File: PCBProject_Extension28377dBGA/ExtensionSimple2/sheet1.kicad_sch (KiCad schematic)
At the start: 109 parts, among them J1 Conn_02x05_Odd_Even, J1 Conn_02x08_Top_Bottom, J2 Conn_01x02_Pin, J5 RS485_1_CONNECT, J7 RS485_2_CONNECT, Q1 FMMT618TA, U1 SN74ABT541, U2 SN74ABT541, U3 SN65HVD75D

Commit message: 解决电流传感器中的错误：电线与边缘太近了！
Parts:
- added C15: 104, Capacitor_SMD:C_0805_2012Metric, symbol sheet1-altium-import:root_1_Cap
- added R48: 4.7k, Resistor_SMD:R_0805_2012Metric, symbol sheet1-altium-import:root_1_Res2
- added U4: SN65HVD230, Package_SO:SOIC-8_3.9x4.9mm_P1.27mm, symbol Interface_CAN_LIN:SN65HVD230
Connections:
- net AGND: now also C15.2, R48.2, U4.2 (GND); no longer C1.1
- net DSP_A_CAN_RX: now also U4.4 (R)
- net DSP_A_CAN_TX: now also U4.1 (D)
- net DSP_PWM1~{_ENABL}E: no longer C1.2
- net VDD: now also C15.1, U4.3 (VCC)
- new net: R48.1, U4.8 (Rs)
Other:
- moved on the sheet: C1

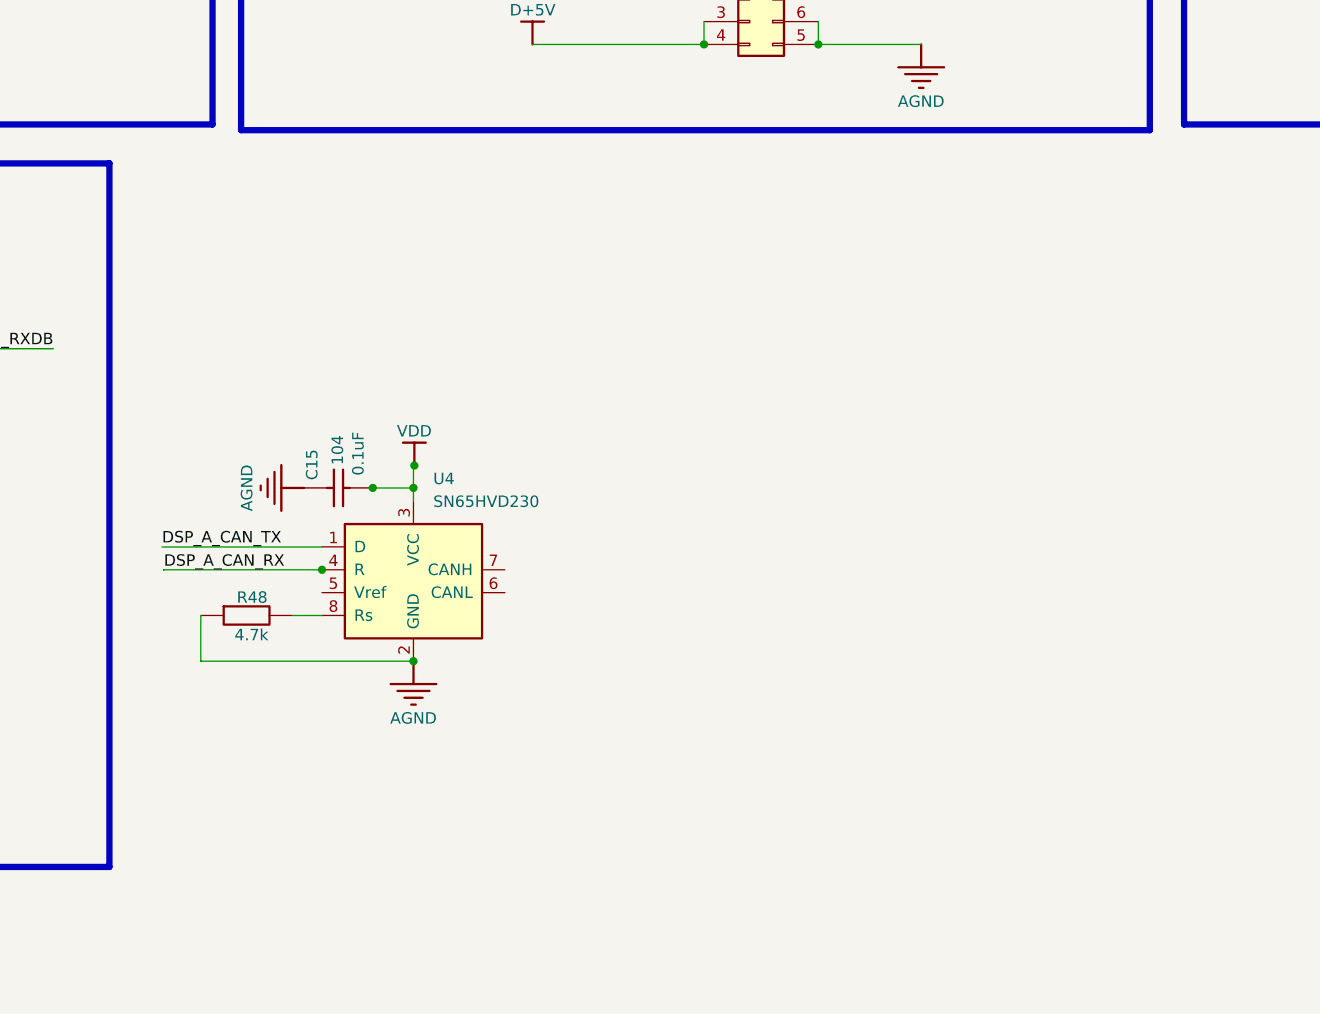
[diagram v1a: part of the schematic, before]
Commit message: 底板中增加了CAN转TTL模块，并初步修改了底板的尺寸
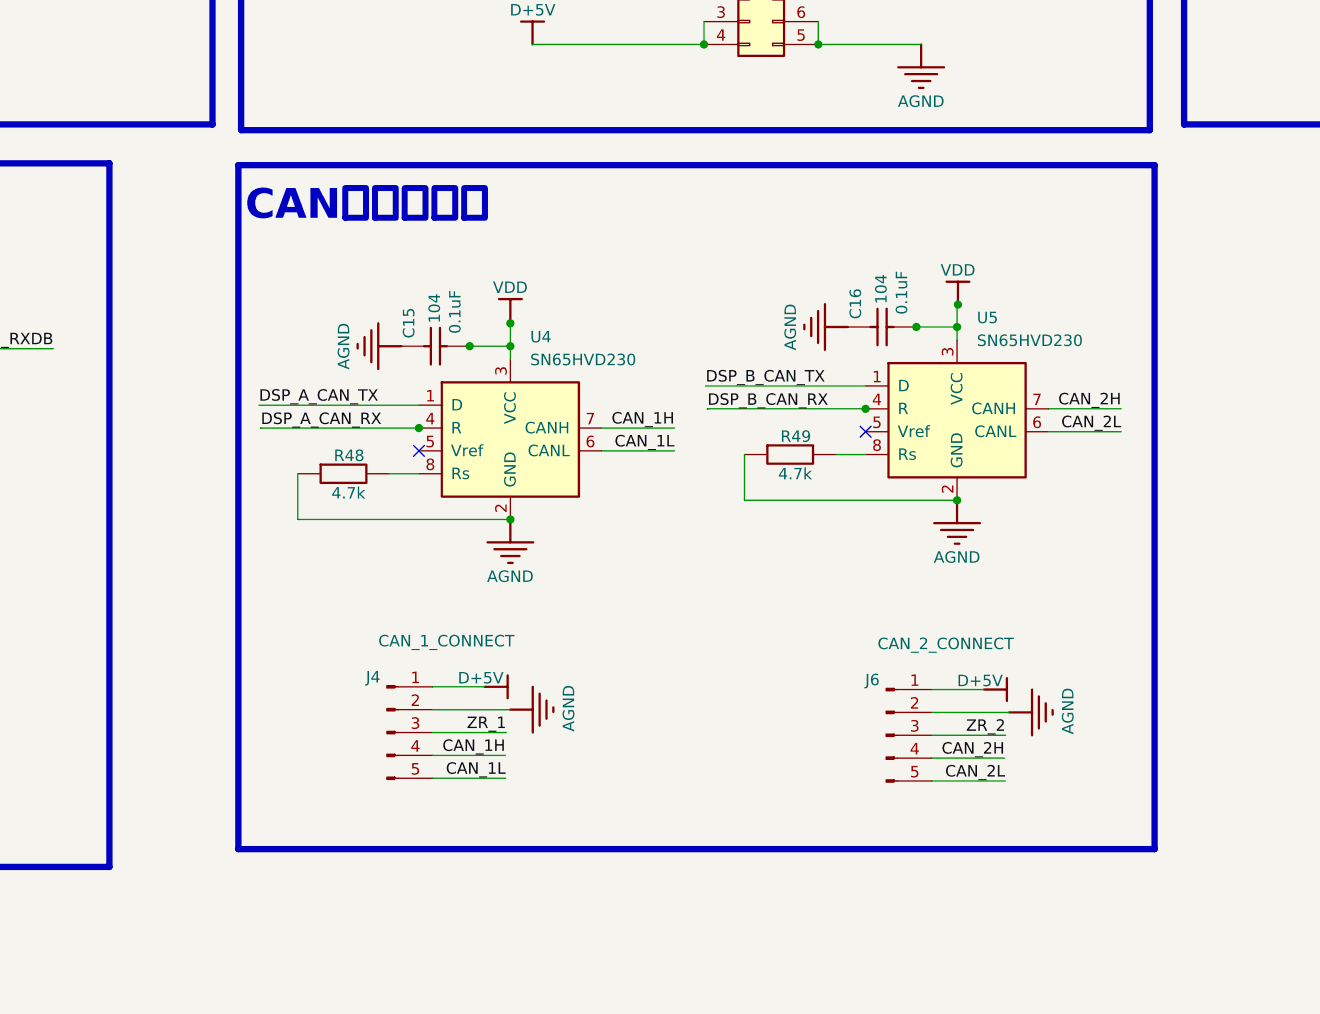
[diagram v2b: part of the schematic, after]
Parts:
- added C16: 104, Capacitor_SMD:C_0805_2012Metric, symbol sheet1-altium-import:root_1_Cap
- added J4: CAN_1_CONNECT, Connector_PinSocket_2.54mm:PinSocket_1x05_P2.54mm_Vertical, symbol Connector:Conn_01x05_Pin
- added J6: CAN_2_CONNECT, Connector_PinSocket_2.54mm:PinSocket_1x05_P2.54mm_Vertical, symbol Connector:Conn_01x05_Pin
- added R49: 4.7k, Resistor_SMD:R_0805_2012Metric, symbol sheet1-altium-import:root_1_Res2
- added U5: SN65HVD230, Package_SO:SOIC-8_3.9x4.9mm_P1.27mm, symbol Interface_CAN_LIN:SN65HVD230
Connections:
- net AGND: now also C16.2, J4.2 (Pin_2), J6.2 (Pin_2), R49.2, U5.2 (GND)
- net D+5V: now also J4.1 (Pin_1), J6.1 (Pin_1)
- net DSP_B_CAN_RX: now also U5.4 (R)
- net DSP_B_CAN_TX: now also U5.1 (D)
- net VDD: now also C16.1, U5.3 (VCC)
- net CAN_1L: now reaches U4.6 (CANL)
- net CAN_1L: now also J4.5 (Pin_5)
- net CAN_1H: now reaches U4.7 (CANH)
- net CAN_1H: now also J4.4 (Pin_4)
- new net: R49.1, U5.8 (Rs)
- new net CAN_2H: J6.4 (Pin_4), U5.7 (CANH)
- new net CAN_2L: J6.5 (Pin_5), U5.6 (CANL)
- new net ZR_1: J4.3 (Pin_3)
- new net ZR_2: J6.3 (Pin_3)
- no-connect marks 84 -> 86
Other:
- note added: "CAN编码器通讯"
- moved on the sheet: C15, R48, U4

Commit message: 确定底板尺寸，目前只差布线
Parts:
- DSP1: footprint Oshinoko:DSP_240_0p6mm -> 1mmlab_pcb_lib:DSP_240_SMD
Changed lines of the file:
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@@
       (effects (font (size 1.27 1.27)))
     )
-    (property "Footprint" "Oshinoko:DSP_240_0p6mm" (at 711.2 421.64 0)
+    (property "Footprint" "1mmlab_pcb_lib:DSP_240_SMD" (at 711.2 421.64 0)
       (effects (font (size 1.27 1.27)) hide)
     )

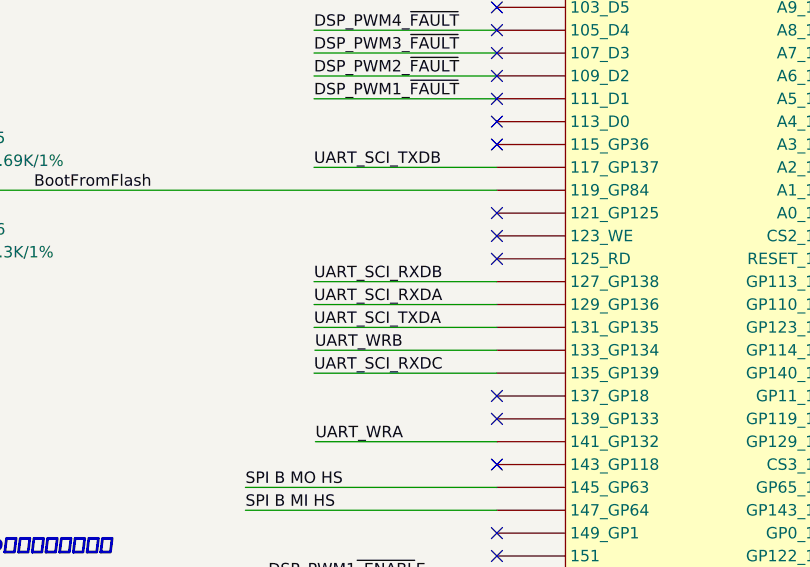
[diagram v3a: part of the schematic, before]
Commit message: 底板布线基本完毕，但是还有些地方出现了混乱，仍需改进
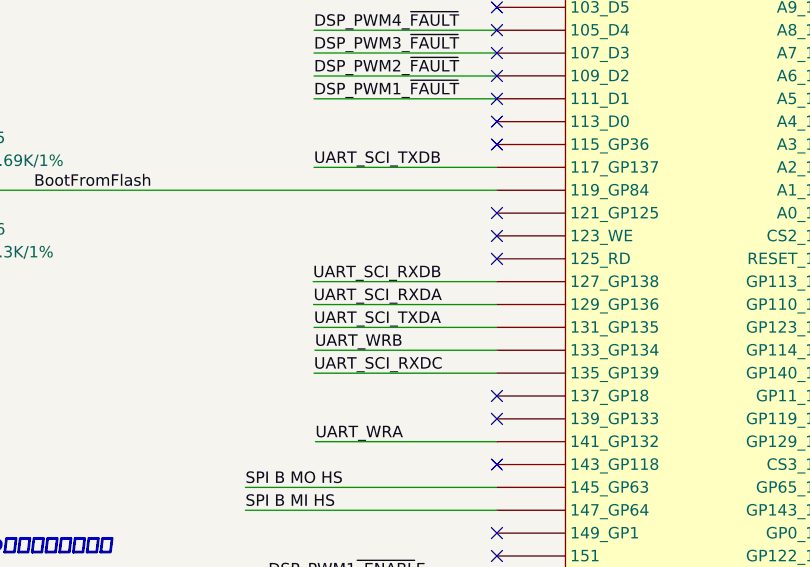
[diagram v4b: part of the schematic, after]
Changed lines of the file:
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@@
+    (stroke (width 0) (type default))
+  )
+  (wire (pts (xy 690.7784 591.82) (xy 711.2 591.82))
     (stroke (width 0) (type default))
   )
@@
     (stroke (width 0.254) (type default))
   )
-  (wire (pts (xy 711.2 594.36) (xy 690.88 594.36))
-    (stroke (width 0.254) (type default))
-  )
   (wire (pts (xy 374.65 70.485) (xy 384.81 70.485))
     (stroke (width 0.254) (type default))
@@
     (stroke (width 0.254) (type default))
   )
+  (wire (pts (xy 690.8292 594.36) (xy 711.2 594.36))
+    (stroke (width 0) (type default))
+  )
   (wire (pts (xy 579.12 268.605) (xy 589.28 268.605))
     (stroke (width 0.254) (type default))
@@
   (wire (pts (xy 346.71 360.045) (xy 346.71 362.585))
     (stroke (width 0) (type default))
-  )
-  (wire (pts (xy 711.2 591.82) (xy 690.88 591.82))
-    (stroke (width 0.254) (type default))
   )
   (wire (pts (xy 756.92 675.64) (xy 770.255 675.64))
@@
     (effects (font (size 1.27 1.27)) (justify left bottom))
   )
+  (label "UART_SCI_RXDA" (at 690.8292 594.36 0) (fields_autoplaced)
+    (effects (font (size 1.27 1.27)) (justify left bottom))
+  )
   (label "RS485_2_B" (at 588.3148 378.6886 180) (fields_autoplaced)
     (effects (font (size 1.27 1.27)) (justify right bottom))
@@
     (effects (font (size 1.27 1.27)) (justify right bottom))
   )
-  (label "UART_SCI_RXDA" (at 690.88 594.36 180) (fields_autoplaced)
-    (effects (font (size 1.27 1.27)) (justify left bottom))
-  )
-  (label "UART_SCI_RXDB" (at 690.88 591.82 180) (fields_autoplaced)
-    (effects (font (size 1.27 1.27)) (justify left bottom))
-  )
   (label "IPM_VDC_BUS1" (at 448.31 67.945 180) (fields_autoplaced)
     (effects (font (size 1.27 1.27)) (justify left bottom))
@@
     (effects (font (size 1.27 1.27)) (justify right bottom))
   )
+  (label "UART_SCI_RXDB" (at 690.7784 591.82 0) (fields_autoplaced)
+    (effects (font (size 1.27 1.27)) (justify left bottom))
+  )
   (label "DSP_B_CAN_TX" (at 693.42 462.28 180) (fields_autoplaced)

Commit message: 底板布线完毕！
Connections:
- net AGND: now also C1.1
- net DSP_PWM1~{_ENABL}E: now also C1.2
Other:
- moved on the sheet: C1
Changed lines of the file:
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@@
   (junction (at 520.7 129.54) (diameter 0) (color 0 0 0 0)
   )
+  (junction (at 106.4006 61.468) (diameter 0) (color 0 0 0 0)
+  )
   (junction (at 520.7 132.08) (diameter 0) (color 0 0 0 0)
   )
@@
     (stroke (width 0) (type default))
   )
+  (wire (pts (xy 115.1382 62.7126) (xy 114.0206 62.7126))
+    (stroke (width 0) (type default))
+  )
   (wire (pts (xy 556.9966 360.7054) (xy 556.9966 360.7562))
     (stroke (width 0) (type default))
   )
+  (wire (pts (xy 81.026 61.468) (xy 106.4006 61.468))
+    (stroke (width 0) (type default))
+  )
   (wire (pts (xy 756.92 629.92) (xy 756.92 632.46))
     (stroke (width 0.254) (type default))
@@
     (stroke (width 0.254) (type default))
   )
+  (wire (pts (xy 114.0206 62.7126) (xy 114.0206 61.468))
+    (stroke (width 0) (type default))
+  )
   (wire (pts (xy 665.48 264.16) (xy 683.26 264.16))
     (stroke (width 0.254) (type default))
@@
     (stroke (width 0) (type default))
   )
+  (wire (pts (xy 106.4006 61.468) (xy 106.426 61.468))
+    (stroke (width 0) (type default))
+  )
   (wire (pts (xy 158.75 140.335) (xy 106.68 140.335))
     (stroke (width 0.254) (type default))
@@
     (effects (font (size 1.27 1.27)) (justify right bottom))
   )
+  (label "DSP_PWM1~{_ENABL}E" (at 81.026 61.468 180) (fields_autoplaced)
+    (effects (font (size 1.27 1.27)) (justify left bottom))
+  )
   (label "DSP-PWM6B" (at 146.05 161.925 180) (fields_autoplaced)
     (effects (font (size 1.27 1.27)) (justify left bottom))
@@
     )
   )
-  (symbol (lib_id "sheet1-altium-import:root_1_Cap") (at 104.14 64.135 90) (unit 1)
+  (symbol (lib_id "sheet1-altium-import:root_1_Cap") (at 111.4806 64.008 90) (unit 1)
     (in_bom yes) (on_board yes) (dnp no)
-    (property "Reference" "C1" (at 103.886 59.309 0)
+    (property "Reference" "C1" (at 109.5502 59.8932 90)
       (effects (font (size 1.27 1.27)) (justify left bottom))
     )
-    (property "Value" "104" (at 106.426 59.309 0)
+    (property "Value" "104" (at 112.4966 66.6242 90)
       (effects (font (size 1.27 1.27)) (justify left bottom))
     )
-    (property "Footprint" "Capacitor_SMD:C_0805_2012Metric" (at 104.14 64.135 0)
+    (property "Footprint" "Capacitor_SMD:C_0805_2012Metric" (at 111.4806 64.008 0)
       (effects (font (size 1.27 1.27)) hide)
     )
-    (property "Datasheet" "" (at 104.14 64.135 0)
+    (property "Datasheet" "" (at 111.4806 64.008 0)
       (effects (font (size 1.27 1.27)) hide)
     )
-    (property "PUBLISHED" "8-Jun-2000" (at 98.552 63.881 0)
+    (property "PUBLISHED" "8-Jun-2000" (at 105.8926 63.754 0)
       (effects (font (size 1.27 1.27)) (justify left bottom) hide)
     )
-    (property "LATESTREVISIONDATE" "17-Jul-2002" (at 98.552 63.881 0)
+    (property "LATESTREVISIONDATE" "17-Jul-2002" (at 105.8926 63.754 0)
       (effects (font (size 1.27 1.27)) (justify left bottom) hide)
     )
-    (property "LATESTREVISIONNOTE" "Re-released for DXP Platform." (at 98.552 63.881 0)
+    (property "LATESTREVISIONNOTE" "Re-released for DXP Platform." (at 105.8926 63.754 0)
       (effects (font (size 1.27 1.27)) (justify left bottom) hide)
     )
-    (property "PACKAGEREFERENCE" "RAD-0.3" (at 98.552 63.881 0)
+    (property "PACKAGEREFERENCE" "RAD-0.3" (at 105.8926 63.754 0)
       (effects (font (size 1.27 1.27)) (justify left bottom) hide)
     )
-    (property "PUBLISHER" "Altium Limited" (at 98.552 63.881 0)
+    (property "PUBLISHER" "Altium Limited" (at 105.8926 63.754 0)
       (effects (font (size 1.27 1.27)) (justify left bottom) hide)
     )
-    (property "ALTIUM_VALUE" "0.1uF" (at 108.966 59.309 0)
+    (property "ALTIUM_VALUE" "0.1uF" (at 112.4966 64.0842 90)
       (effects (font (size 1.27 1.27)) (justify left bottom))
     )
@@
     )
   )
-  (symbol (lib_id "sheet1-altium-import:AGND") (at 106.68 66.675 0) (unit 1)
+  (symbol (lib_id "sheet1-altium-import:AGND") (at 115.1382 62.7126 90) (unit 1)
     (in_bom yes) (on_board yes) (dnp no)
-    (property "Reference" "#PWR01" (at 106.68 66.675 0)
+    (property "Reference" "#PWR01" (at 115.1382 62.7126 0)
       (effects (font (size 1.27 1.27)) hide)
     )
-    (property "Value" "AGND" (at 106.68 73.025 0)
+    (property "Value" "AGND" (at 121.4882 62.7126 0)
       (effects (font (size 1.27 1.27)))
     )
-    (property "Footprint" "" (at 106.68 66.675 0)
+    (property "Footprint" "" (at 115.1382 62.7126 0)
       (effects (font (size 1.27 1.27)) hide)
     )
-    (property "Datasheet" "" (at 106.68 66.675 0)
+    (property "Datasheet" "" (at 115.1382 62.7126 0)
       (effects (font (size 1.27 1.27)) hide)
     )
